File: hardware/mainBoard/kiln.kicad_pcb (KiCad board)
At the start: 4 copper layers, 203.1 x 114.5 mm, 214 parts, among them IC4 MAXM17572AMC+T, IC5 MAXM17572AMC+T, IC6 MAXM17572AMC+T, IC7 MAXM17572AMC+T, J1 1935161, J10 1935174, J11 1935174, J12 1935161, J13 SJ2-35813B-SMT-TR, J14 1935161, J15 SJ2-35813B-SMT-TR, J16 1935161, J17 SJ2-35813B-SMT-TR, J18 1935161, J19 1935161, J2 Conn_01x10_Pin, J20 1935161, J21 1935161, J23 1935161, J24 1935161, J25 1935161, J3 1935174, J4 1935174, J6 Conn_01x20_Socket, J7 Conn_02x06_Odd_Even, J8 1935174, K1 EE2-12NUH, K2 EE2-12NUH, K3 EE2-12NUH, K4 EE2-12NUH, K5 EE2-12NUH, Q1 BSS138P,215, Q2 BSS138P,215, Q3 BSS138P,215, Q4 BSS138P,215, Q5 BSS138P,215, U1 TCMT1109, U13 TCMT1109, U14 TCMT1109, U2 TCMT1109, U3 TCMT1109, U4 ESP32-S3-DevKitC, U5 SX1509, U7 AD8542, U8 AD8542, U9 AD8542

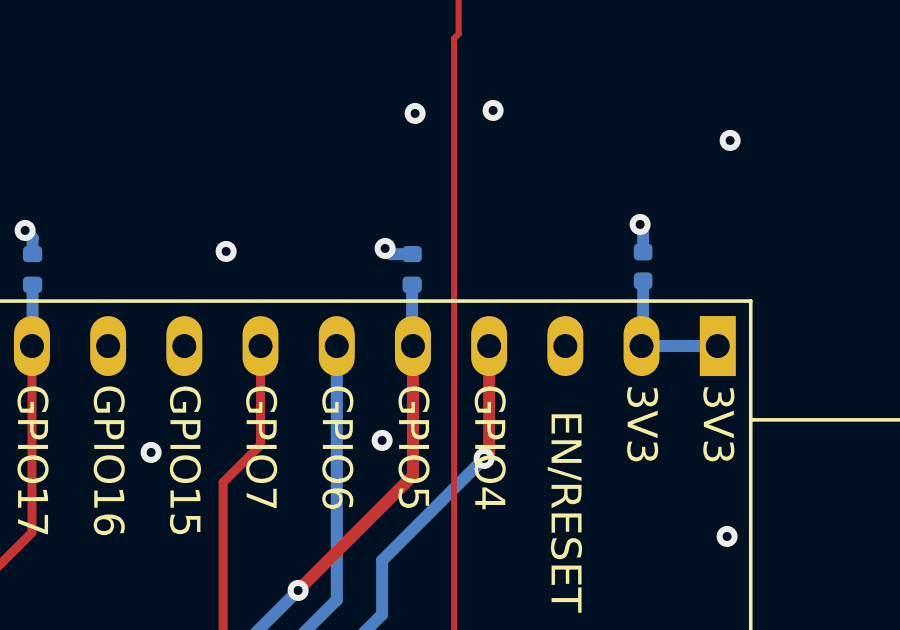
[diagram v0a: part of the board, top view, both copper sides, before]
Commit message: Safety link: the isolated UART pin map, measured instead of traced
The ESP's safety-link TX/RX were swapped relative to the board, and had
been since the pin defaults were set. The link could not work in either
direction: the ESP transmitted into U3's collector and listened on U2's
LED drive. Correct map, now measured on the bench rather than derived
from the schematic:

  ESP GPIO5 = TX (DataToSafty, drives U2's LED through R12)
  ESP GPIO4 = RX (DataFromSafty, U3's collector, R15 pull-up)

Schematic and board
-------------------
Three faults, all fixed here and reworked on the physical board:

  - The top-level sheet crossed the two hierarchical pins: MainControler's
    DataToSafty (an output) was wired to SaftyProcessor's DataFromSafty
    (also an output), and the two inputs were wired to each other. That
    collapsed the two names into one net, which KiCad named after the
    main sheet, so the same wire appeared under both names depending on
    which sheet you read.
  - The MainControler sheet's labels were swapped relative to the safety
    sheet's. They now agree: U3's collector is DataFromSafty everywhere,
    R12's net is DataToSafty everywhere.
  - R15 (1k to 3.3V_Main) sat on the TX net, where a pull-up does nothing,
    while the RX collector had none. Moved onto GPIO4, mirroring R9's role
    on the safety side.

The measurement
---------------
Coordinated two-board GPIO test, each processor reached by a path that is
not the link under test (ESP over its USB-serial bridge and JTAG, Pico
over SWD). Every crossing inverts, as predicted:

  ESP GPIO5 high  -> Pico GP5 low    (U2's LED lit)
  ESP GPIO5 low   -> Pico GP5 high   (R9 pulls up)
  Pico GP4 high   -> ESP GPIO4 low   (U3's LED lit)
  Pico GP4 low    -> ESP GPIO4 high  (R15 pulls up)
  Pico GP5 driven -> no change at the ESP (its own receiver)
  ESP GPIO6 high  -> Pico GP10 low   (U1's LED lit)
  ESP in reset    -> Pico GP10 high  (R8 pulls up)

Corroborated at register level: ESP GPIO_IN_REG 0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
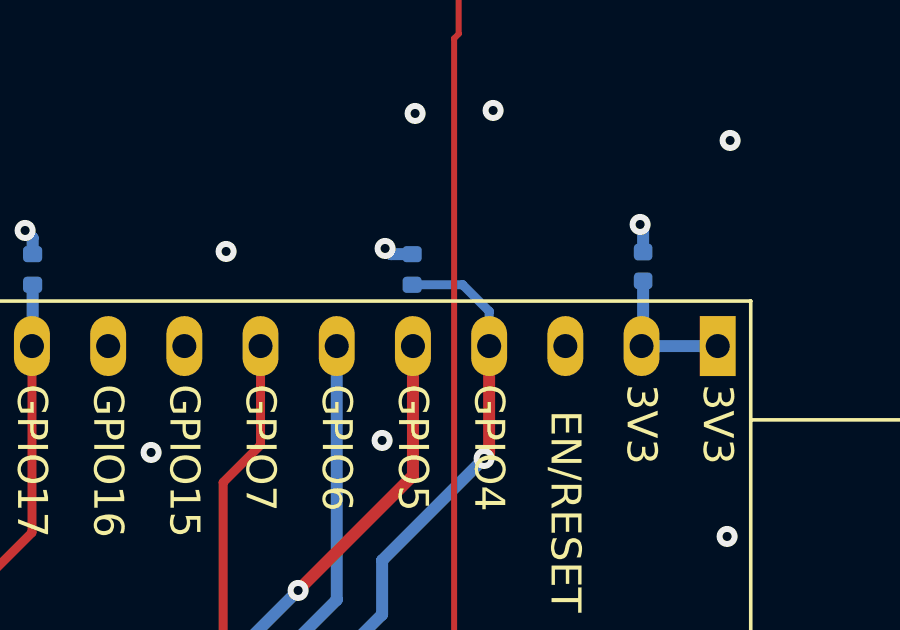
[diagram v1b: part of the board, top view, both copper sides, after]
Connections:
- R12 pad 1: /MainControler/DataFromSafty -> /MainControler/DataToSafty
- U3 pad 4: /MainControler/DataToSafty -> /MainControler/DataFromSafty
- U4 pad 4: /MainControler/DataToSafty -> /MainControler/DataFromSafty
- U4 pad 5: /MainControler/DataFromSafty -> /MainControler/DataToSafty
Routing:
- net /MainControler/DataFromSafty: track 127.0 -> 132.2 mm
- net /MainControler/DataToSafty: track 128.1 -> 125.0 mm
